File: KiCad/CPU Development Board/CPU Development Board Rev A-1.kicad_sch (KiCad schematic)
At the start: 29 parts, among them J1 Micro USB, J2 Debug, J3 Power Select Jumper, J4 Conn_01x16_Pin, J5 Conn_01x16_Pin, J6 Boot Select, SW1 Reset, U1 STM32L151C8T6, U2 AMS1117-3.3, Y1 16 MHz

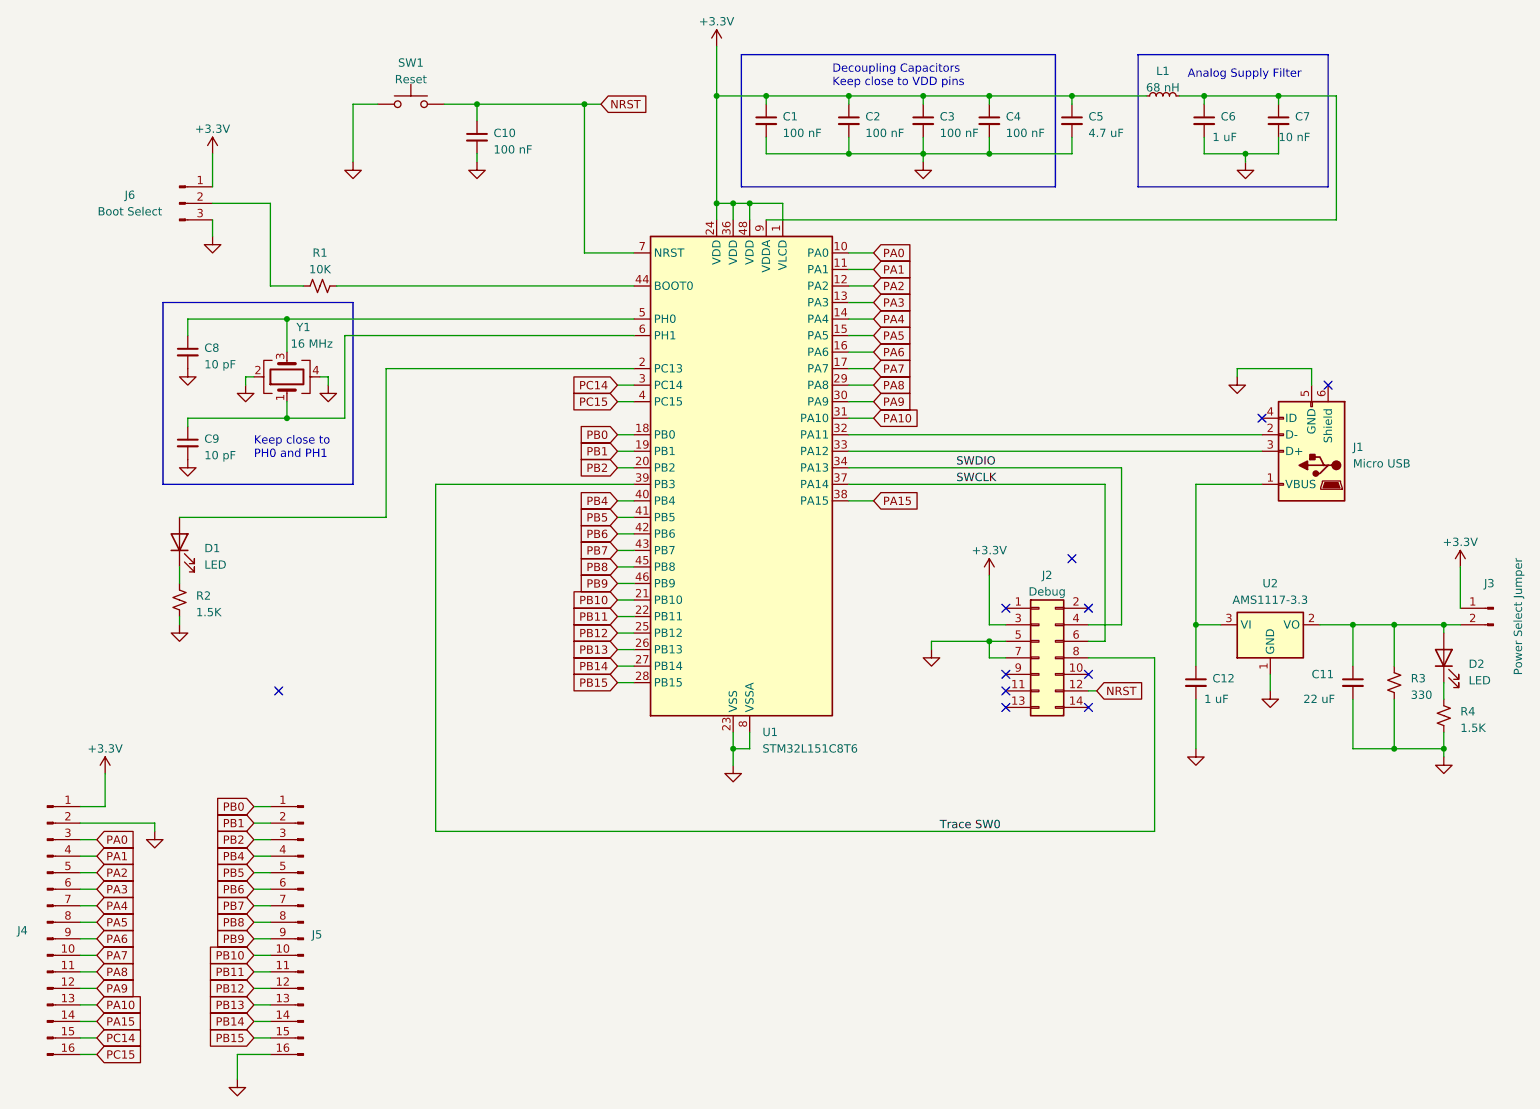
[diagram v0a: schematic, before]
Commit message: Updated CPU schematic for 14 pin debug connector
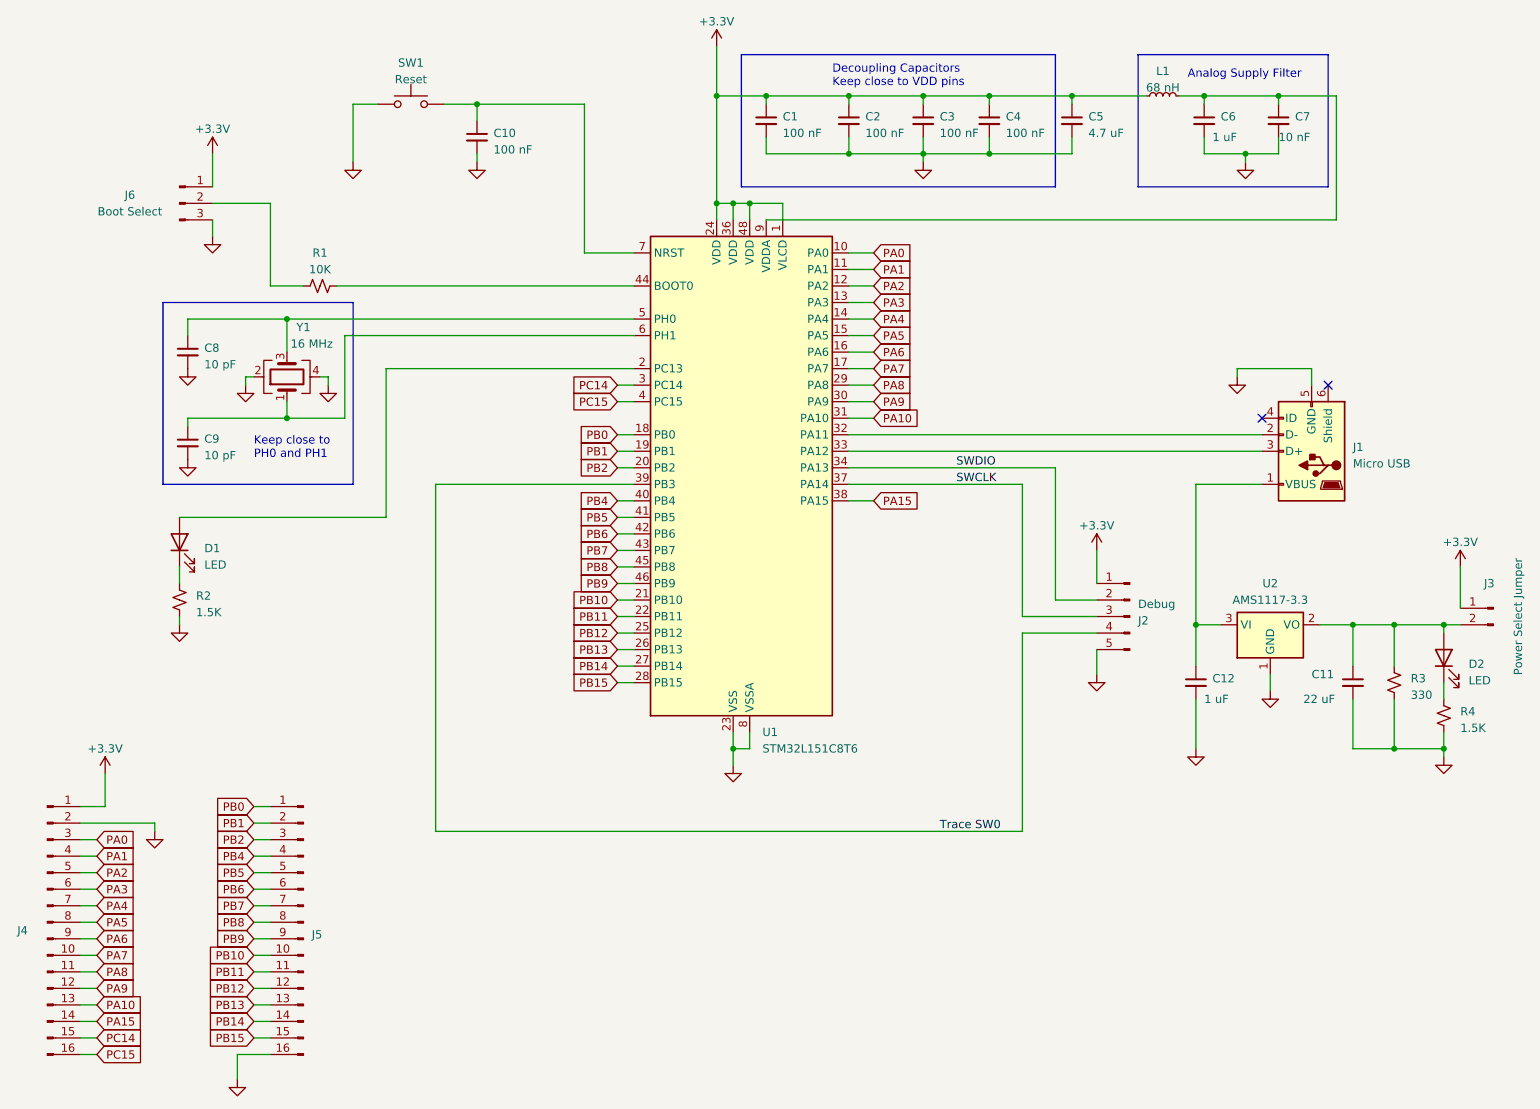
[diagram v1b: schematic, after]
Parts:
- removed J2: Debug, symbol Connector_Generic:Conn_02x07_Odd_Even
- added J2: Debug, symbol Connector:Conn_01x05_Pin
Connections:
- net +3.3V: now also J2.1 (Pin_1)
- net GND: now also J2.5 (Pin_5)
- net SWCLK: now also J2.3 (Pin_3)
- net SWDIO: now also J2.2 (Pin_2)
- net Trace SW0: now also J2.4 (Pin_4)
- net NRST: no longer names the net of C10.1, SW1.2, U1.7 (NRST)
- no-connect marks 11 -> 2
